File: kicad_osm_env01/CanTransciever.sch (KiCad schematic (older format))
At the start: 24 parts, among them U8 SN65HVD230

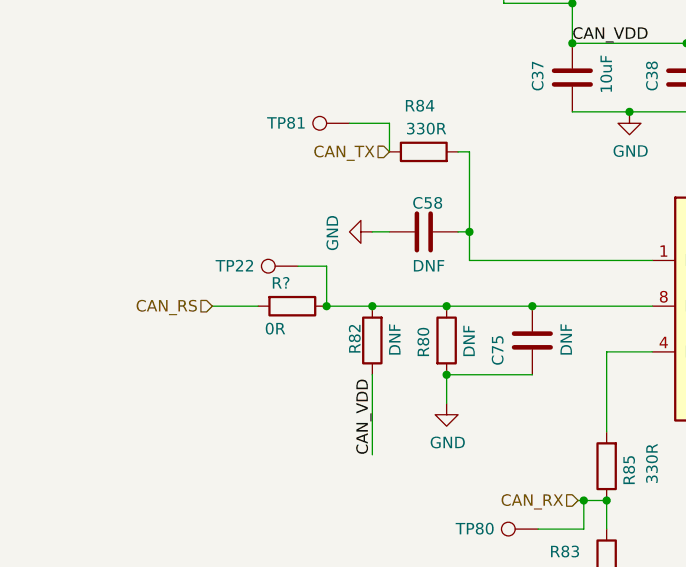
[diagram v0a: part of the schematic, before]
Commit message: updated schematics
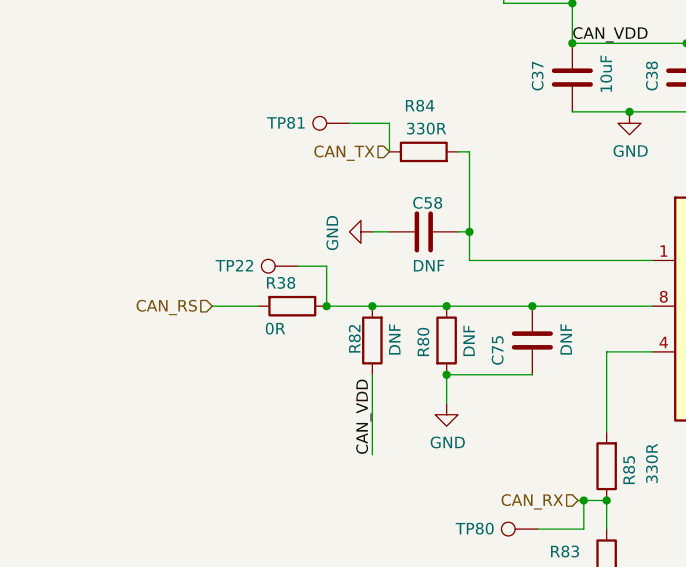
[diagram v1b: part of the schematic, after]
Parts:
- gave numbers to parts that had none: 1
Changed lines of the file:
@@
 $Descr A4 11693 8268
 encoding utf-8
-Sheet 9 9
+Sheet 7 9
 Title ""
 Date ""
@@
 	7675 3975 7825 3975
 $Comp
-L device:R R?
+L device:R R38
 U 1 1 614A8ACA
 P 3925 4000
-F 0 "R?" V 3825 3950 50  0000 C CNN
+F 0 "R38" V 3825 3950 50  0000 C CNN
 F 1 "0R" V 4025 3925 50  0000 C CNN
 F 2 "" V 3855 4000 50  0001 C CNN

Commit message: Updated schematics
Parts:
- removed R23: 0R, Resistor_SMD:R_0603_1608Metric, symbol device:R
- removed R24, R80, R82: DNF, Resistor_SMD:R_0603_1608Metric, symbol device:R
- added L6: 2A/0.05DCR, Inductor_SMD:L_0402_1005Metric, symbol device:Ferrite_Bead
- C79: value C -> DNF
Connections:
- net +3V3: now also L6.2
- net CAN_VDD: no longer names the net of C37.2, C38.2, R31.2, U8.3 (VCC)
- net CAN_VDD: now also L6.1
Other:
- moved on the sheet: C58, C75, R38, R83, R84, R85, TP22, TP80, TP81

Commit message: rough throwdown of all parts
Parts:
- C37: footprint Capacitor_SMD:C_0805_2012Metric -> Capacitor_SMD:C_0603_1608Metric
- R38: footprint (none) -> Resistor_SMD:R_0603_1608Metric
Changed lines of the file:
@@
 F 0 "C37" V 5300 2925 50  0000 L CNN
 F 1 "10uF" V 5000 2900 50  0000 L CNN
-F 2 "Capacitor_SMD:C_0805_2012Metric" H 5188 2850 50  0001 C CNN
+F 2 "Capacitor_SMD:C_0603_1608Metric" H 5188 2850 50  0001 C CNN
 F 3 "" H 5150 3000 50  0001 C CNN
 	1    5150 3000
@@
 F 0 "R38" V 4225 4000 50  0000 C CNN
 F 1 "0R" V 4300 4000 50  0000 C CNN
-F 2 "" V 4305 4000 50  0001 C CNN
+F 2 "Resistor_SMD:R_0603_1608Metric" V 4305 4000 50  0001 C CNN
 F 3 "" H 4375 4000 50  0001 C CNN
 	1    4375 4000
